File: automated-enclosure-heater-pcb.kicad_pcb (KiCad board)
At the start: 2 copper layers, 78 x 90 mm, 63 parts, among them J1 PowerPole Power in, J2 Servo, J3 RJ45, J4 Buttons, J5 DS18B20 Heater, J6 DS18B20 Case, J7 PowerPole Heater Connector, J8 JST-XH Fan Connector, K1 G5LE-1A, K2 G5LE-1A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

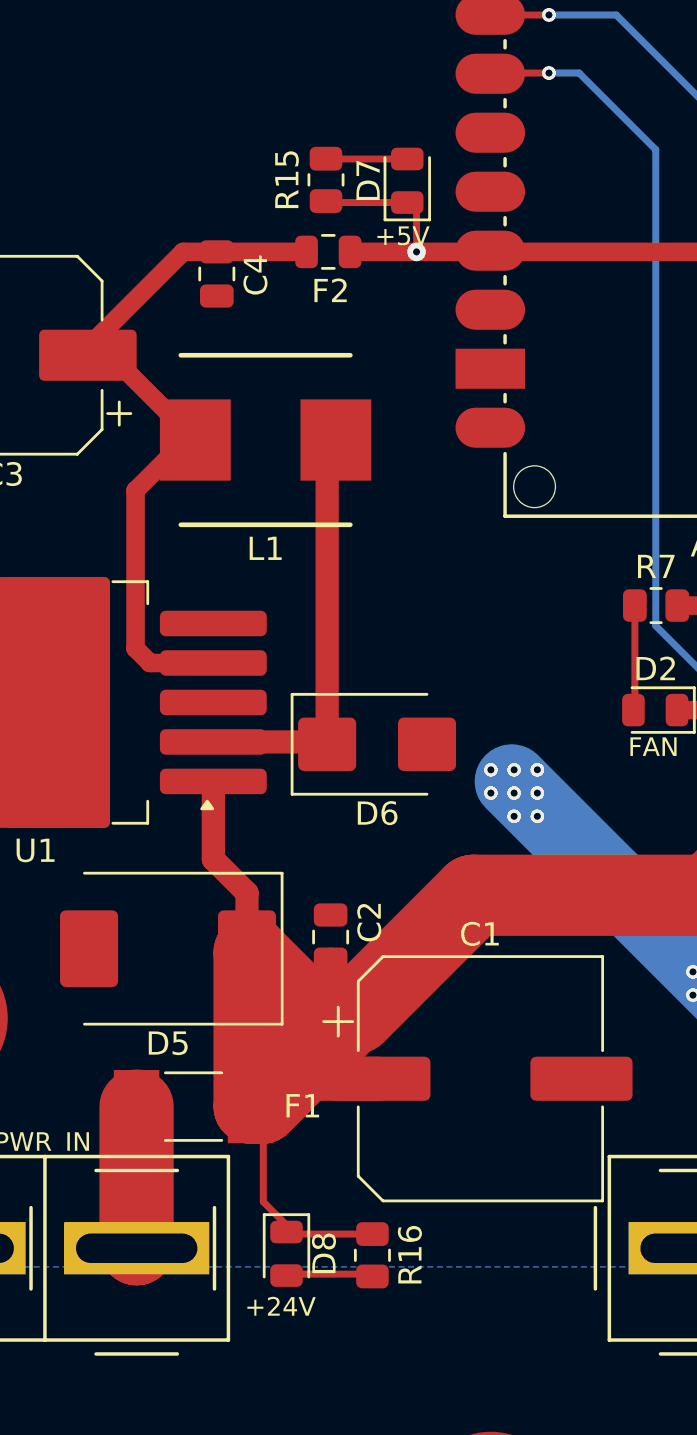
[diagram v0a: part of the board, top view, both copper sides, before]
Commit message: Fix LED issue
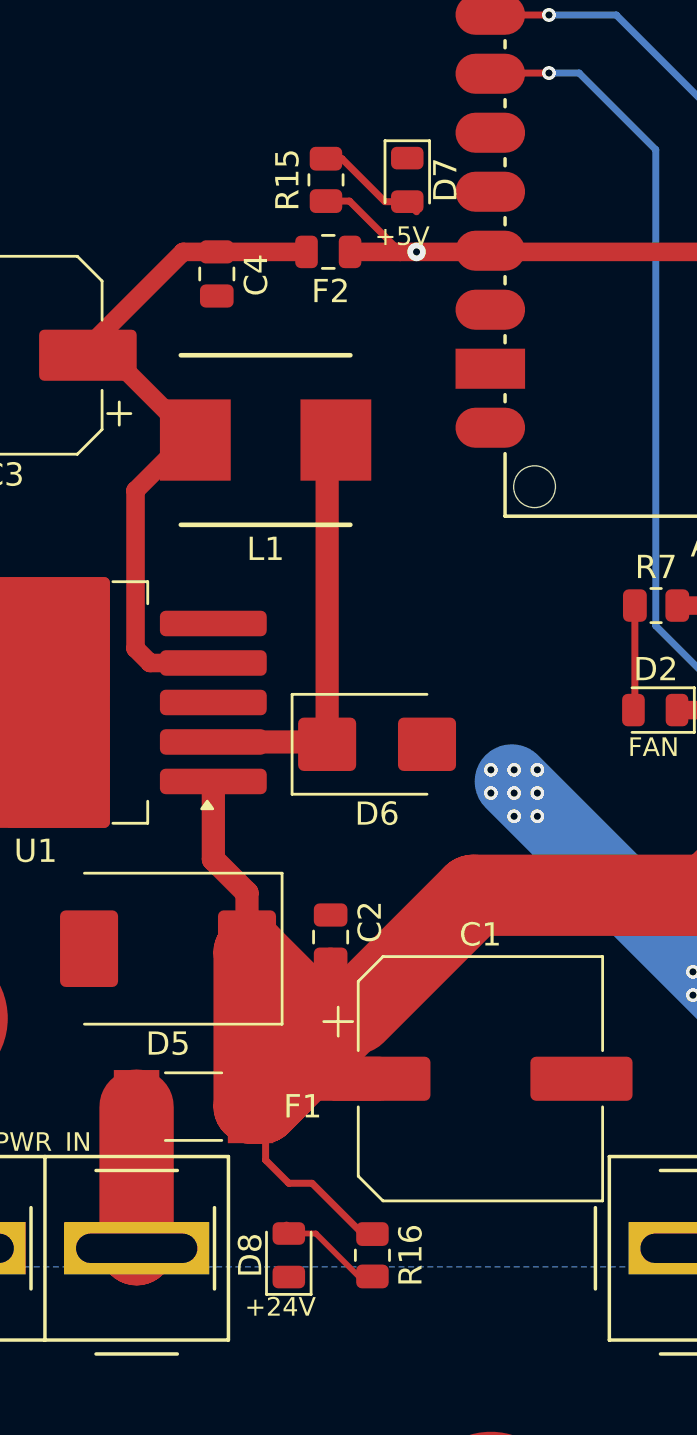
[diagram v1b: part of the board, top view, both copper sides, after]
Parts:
- moved D8 0.12 mm to (195.5, 122.6), turned to 90 degrees
- turned D7 to -90 degrees
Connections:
- D7 pad 1: +5V -> GND
- D8 pad 1: +24V -> GND
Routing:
- net +5V: track 89.0 -> 87.4 mm
- net +24V: track 101.1 -> 99.6 mm
- net Net-(D7-A): track 3.51 -> 4.89 mm
- net Net-(D8-A): track 3.98 -> 4.93 mm

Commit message: Add minor silkscreen adjustments
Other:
- board text added: "HEATER"
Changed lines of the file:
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@@
 			)
 		)
+		(property "Purpose" "HEATER"
+			(at 0 0 180)
+			(unlocked yes)
+			(layer "F.Fab")
+			(hide yes)
+			(effects
+				(font
+					(size 1 1)
+					(thickness 0.15)
+				)
+			)
+		)
 		(property ki_fp_filters "LED* LED_SMD:* LED_THT:*")
 		(sheetname "Root")
@@
 			)
 		)
+		(property "Purpose" "FAN"
+			(at 0 0 90)
+			(unlocked yes)
+			(layer "F.Fab")
+			(hide yes)
+			(effects
+				(font
+					(size 1 1)
+					(thickness 0.15)
+				)
+			)
+		)
 		(property ki_fp_filters "LED* LED_SMD:* LED_THT:*")
 		(sheetname "Root")
@@
 		)
 	)
-	(gr_text "FAN"
-		(at 210.1 101.2 0)
+	(gr_text "HEATER"
+		(at 208.5 101.5 0)
 		(layer "F.SilkS")
 		(effects
 			(font
-				(size 0.8 0.8)
-				(thickness 0.125)
+				(size 1 1)
+				(thickness 0.15)
 			)
 			(justify left bottom)
@@
 	)
 	(gr_text "FAN"
-		(at 239.1 86.3 90)
+		(at 239 86.6 90)
 		(layer "F.SilkS")
 		(effects
 			(font
-				(size 0.8 0.8)
-				(thickness 0.125)
+				(size 1 1)
+				(thickness 0.15)
 			)
 			(justify left bottom)

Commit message: Fix DISP pinout
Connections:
- J3 pad 1: /DISPLAY_SDA_OUT -> GND
- J3 pad 2: GND -> /DISPLAY_SDA_OUT
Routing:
- net /DISPLAY_SDA_OUT: track 12.6 -> 12.1 mm, vias 0 -> 1

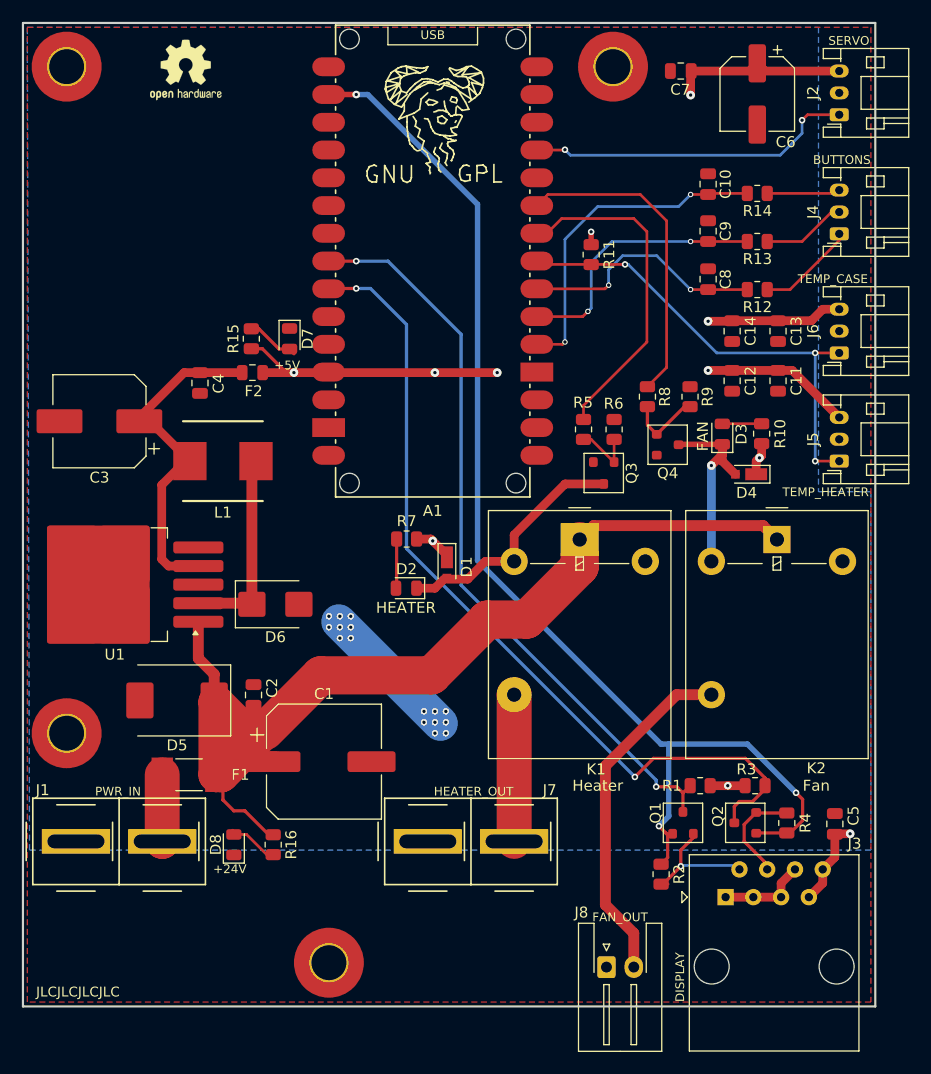
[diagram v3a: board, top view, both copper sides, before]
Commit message: Adjust Arduino pinout and push version to v0.2
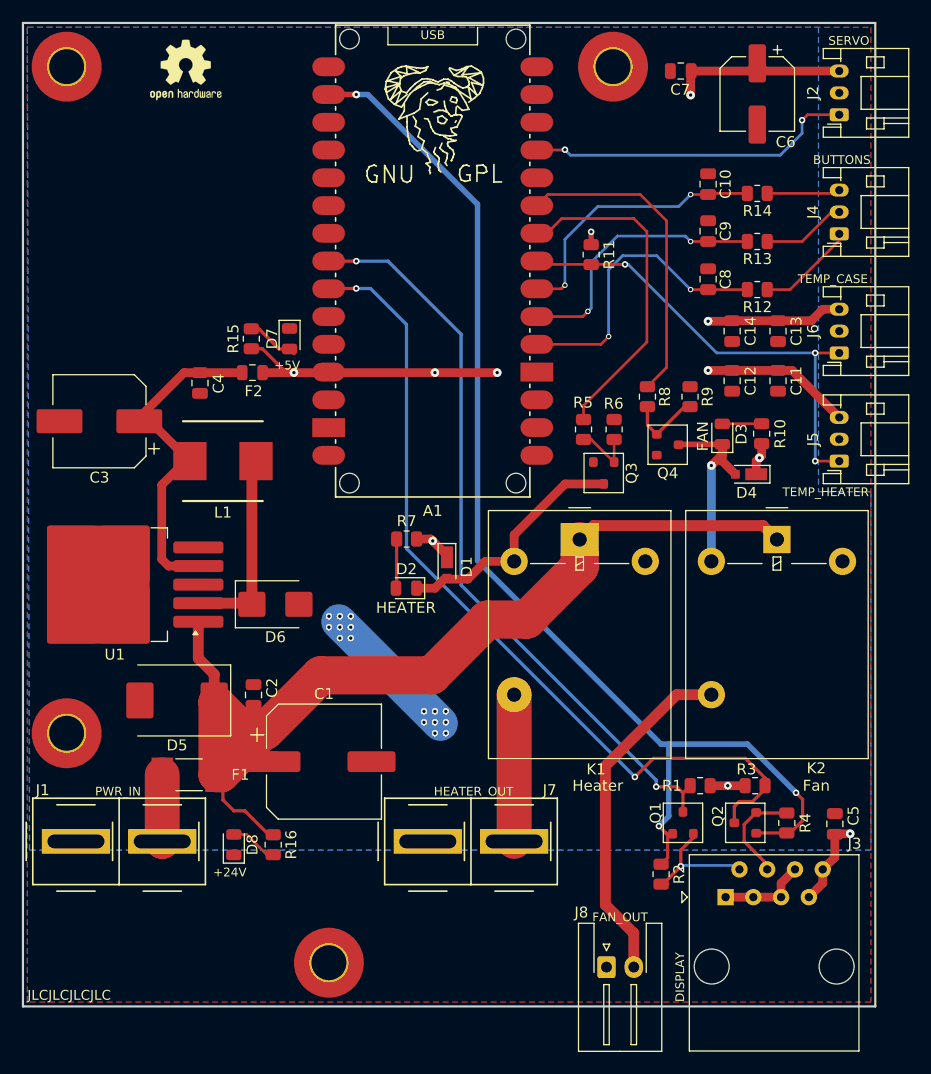
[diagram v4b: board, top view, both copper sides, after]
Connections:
- A1 pad D2: /BUTTON_UP_GPIO -> /BUTTON_DOWN_GPIO
- A1 pad D4: /BUTTON_DOWN_GPIO -> /BUTTON_UP_GPIO
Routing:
- net /BUTTON_UP_GPIO: track 30.5 -> 25.3 mm
- net /BUTTON_DOWN_GPIO: track 22.6 -> 27.5 mm

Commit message: Add second resistor for 24V LED and adjust power plane size
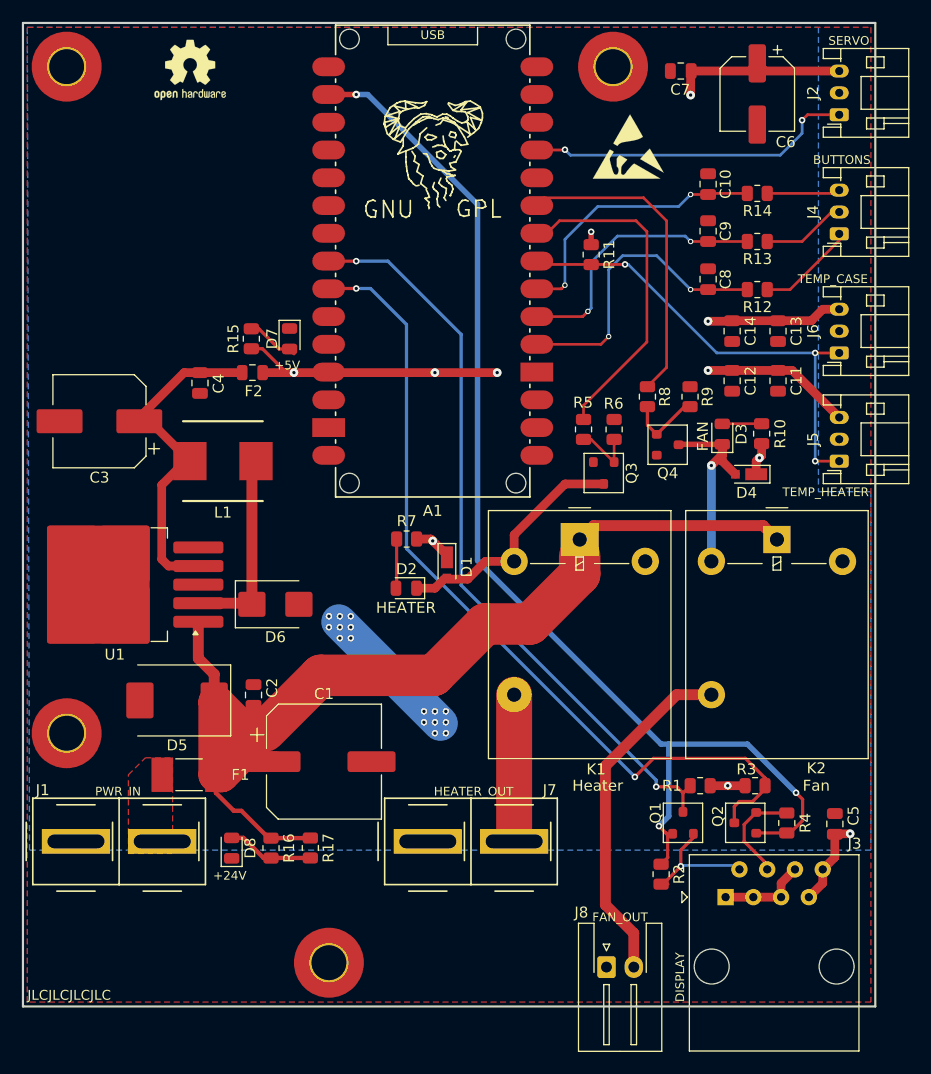
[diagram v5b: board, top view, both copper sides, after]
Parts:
- added R17: 4.5k, Resistor_SMD:R_0805_2012Metric, F.Cu at (202.5, 122.9)
- added REF**: ESD-Logo_6.6x6mm_SilkScreen, Symbol:ESD-Logo_6.6x6mm_SilkScreen, F.Cu at (231.6, 58.7)
- R16: value 2.2k -> 4.5k
- moved REF** 3.20 mm to (214.0, 58.3)
- moved REF** 0.40 mm to (191.5, 51.7)
- moved D8 0.37 mm to (195.3, 122.9)
- moved R16 0.37 mm to (198.9, 122.9)
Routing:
- net /PWR_IN: track 6.10 -> 0.00 mm
- net +24V: track 99.6 -> 103.0 mm
- net Net-(D8-A): track 4.93 -> 7.97 mm
- net /HEATER_OUT: track 13.4 -> 12.3 mm
- added copper zone on F.Cu, net /PWR_IN
